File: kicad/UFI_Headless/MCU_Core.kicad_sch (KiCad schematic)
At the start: 43 parts, among them J4 SWD, J5 DBG_UART, SW1 RESET, SW2 BOOT, U5 STM32H723ZGT6, Y1 25MHz CL=8pF

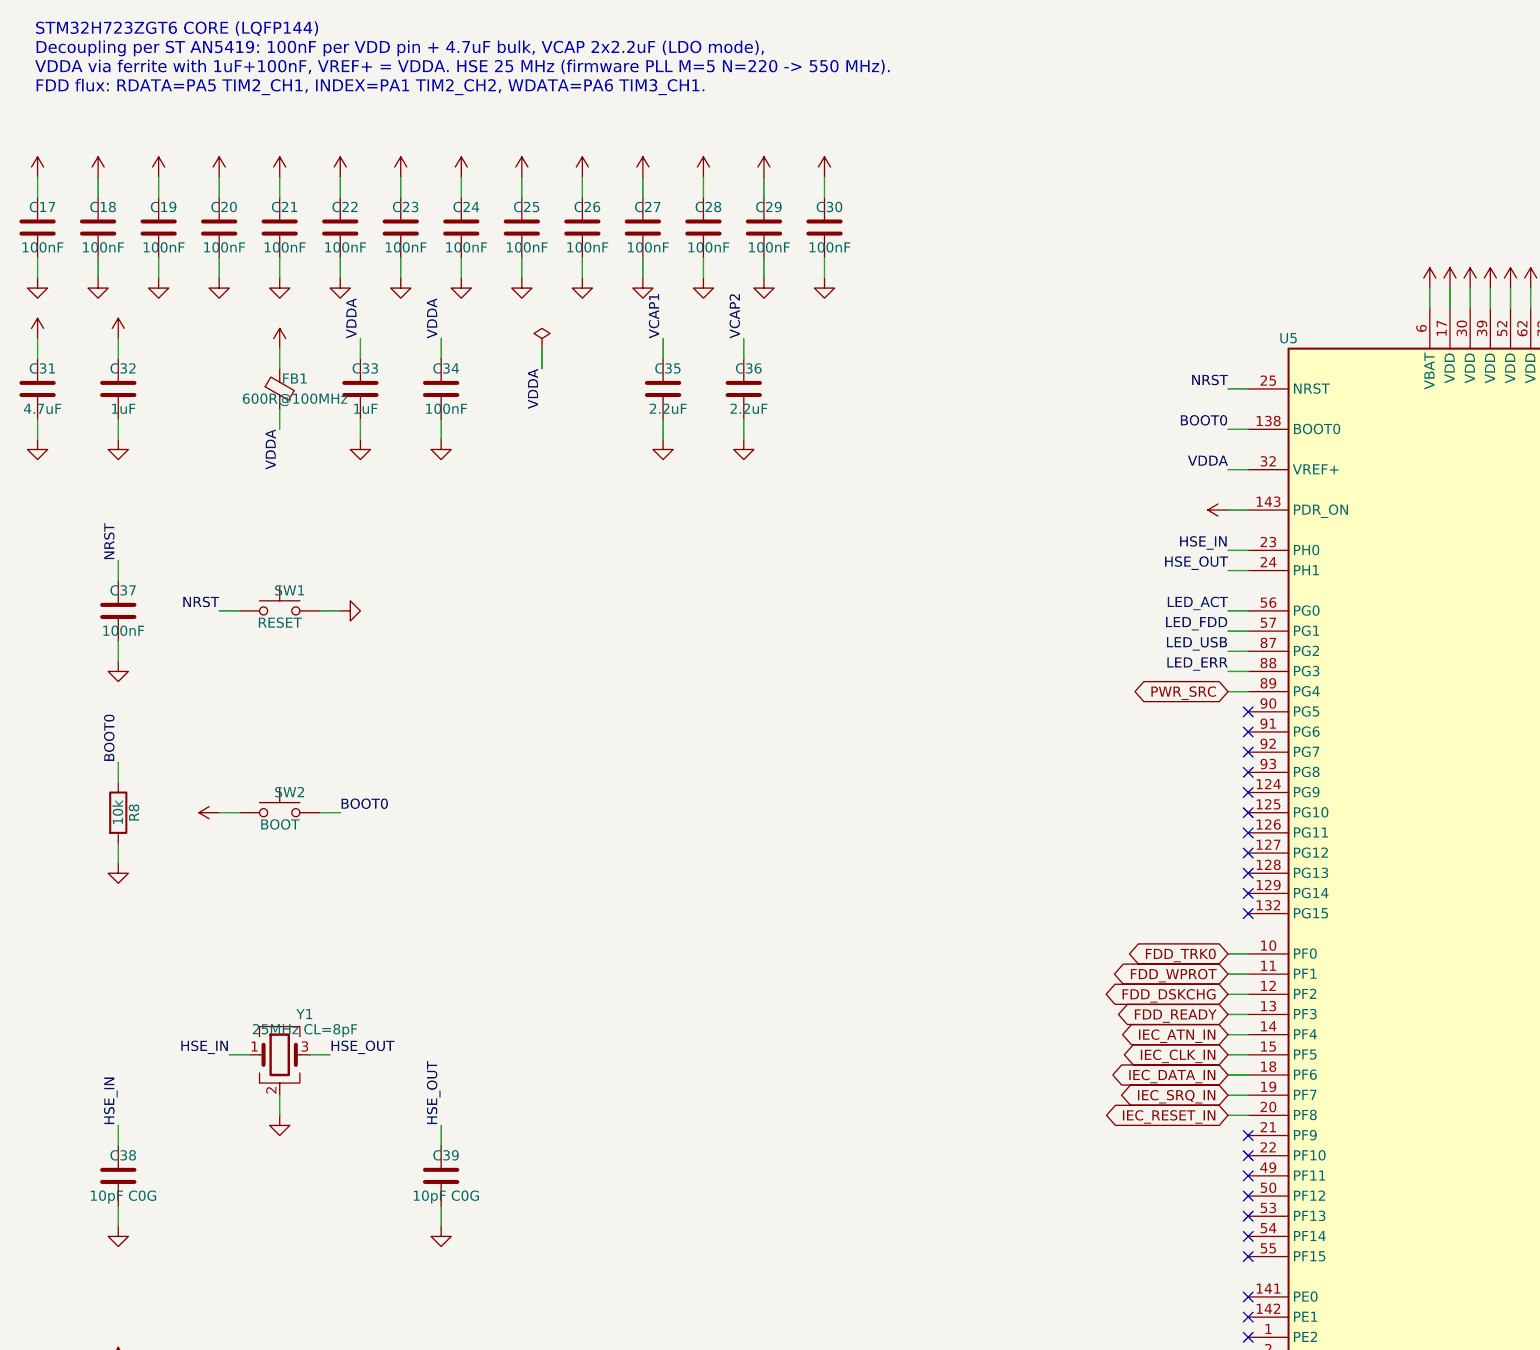
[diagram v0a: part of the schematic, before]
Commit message: UFI Headless: 4-layer layout v0.1, LCSC sourcing, fab outputs
- build_pcb.py: footprints from the schematic netlist (KIID-linked), placement,
  pre-routed USB-C fan-out and MCU VSS stubs, In1 GND plane
- make_pcb.sh: Freerouting 2.4.1 routing, violation cleanup, supply widening,
  GND/3V3 pours, stitching vias; DRC 0 errors, schematic parity clean
- LCSC part numbers via JLCPCB API; crystal X322525MOB4SI (CL 12pF, 2x 18pF)
- fertigung/: Gerber, Excellon, BOM/CPL (KiCad + JLC format)

Co-Authored-By: Claude Opus 5.5 <noreply@anthropic.com>
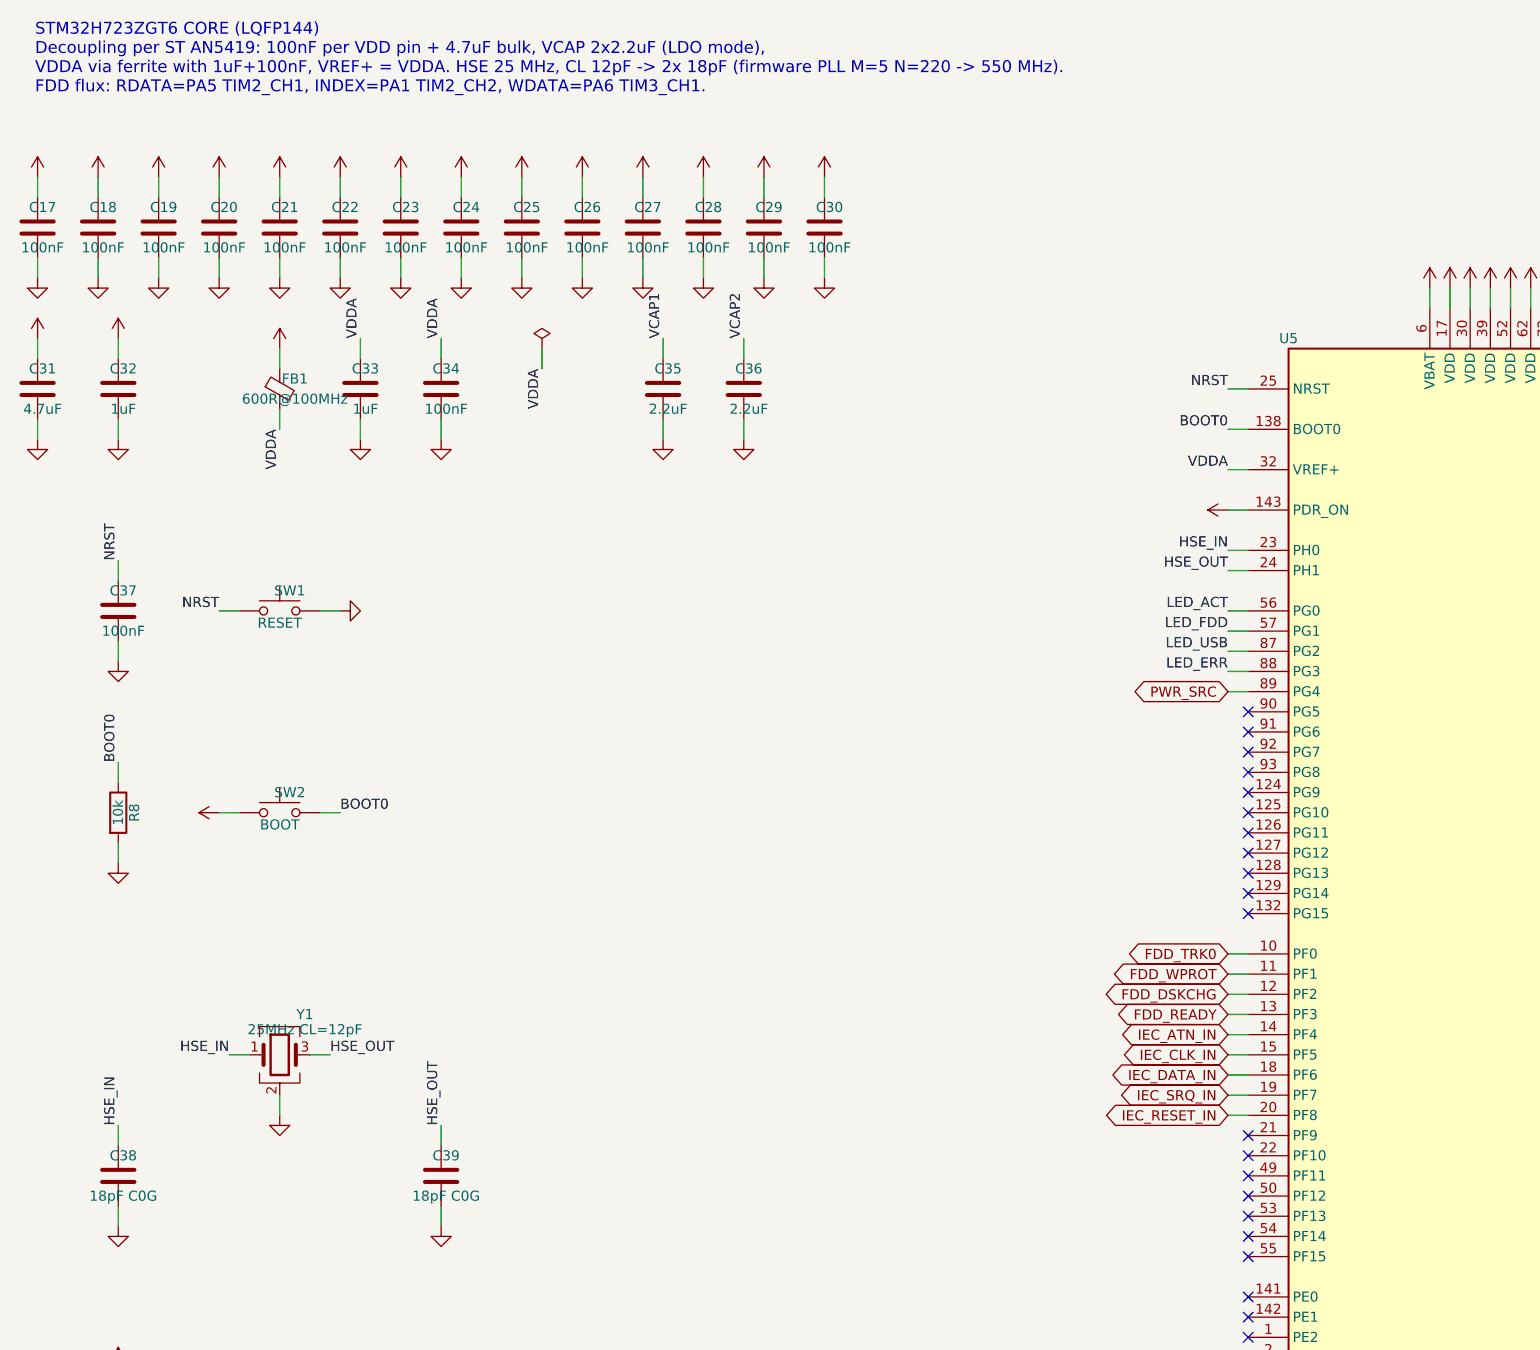
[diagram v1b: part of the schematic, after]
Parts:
- C17, C18, C19, C20, C21, C22, C23, C24, C25, C26, C27, C28, C29, C30, C34, C37: LCSC (none) -> C14663
- C31: LCSC (none) -> C1779
- C32: LCSC (none) -> C28323
- C33: LCSC (none) -> C15849
- C35, C36: LCSC (none) -> C87994
- C38, C39: value 10pF C0G -> 18pF C0G; LCSC (none) -> C1647
- D4, D5, D6, D8: LCSC (none) -> C12624
- D7: LCSC (none) -> C2286
- FB1: LCSC (none) -> C1002
- J4: LCSC (none) -> C22438120
- J5: LCSC (none) -> C49257
- R10: LCSC (none) -> C4216
- R11, R12, R13, R14: LCSC (none) -> C21190
- R15: LCSC (none) -> C4190
- R8: LCSC (none) -> C25804
- R9: LCSC (none) -> C31850
- SW1, SW2: LCSC (none) -> C2886898
- U5: LCSC (none) -> C730146
- Y1: value 25MHz CL=8pF -> 25MHz CL=12pF; LCSC (none) -> C9006; MPN 25MHz 3225 CL=8pF +-20ppm -> YXC X322525MOB4SI (25MHz, CL 12pF, +-10ppm)
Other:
- note added: "STM32H723ZGT6 CORE (LQFP144) Decoupling per ST AN5419: 100nF per VDD pin + 4.7uF bulk, VCAP 2x2.2uF (LDO mode), VDDA via ferrite with 1uF+100nF, VREF+ = VDDA. HSE 25 MHz, CL 12pF -> 2x 18pF (firmware PLL M=5 N=220 -> 550 MHz). FDD flux: RDATA=PA5 TIM2_CH1, INDEX=PA1 TIM2_CH2, WDATA=PA6 TIM3_CH1."
- note removed: "STM32H723ZGT6 CORE (LQFP144) Decoupling per ST AN5419: 100nF per VDD pin + 4.7uF bulk, VCAP 2x2.2uF (LDO mode), VDDA via ferrite with 1uF+100nF, VREF+ = VDDA. HSE 25 MHz (firmware PLL M=5 N=220 -> 550 MHz). FDD flux: RDATA=PA5 TIM2_CH1, INDEX=PA1 TIM2_CH2, WDATA=PA6 TIM3_CH1."

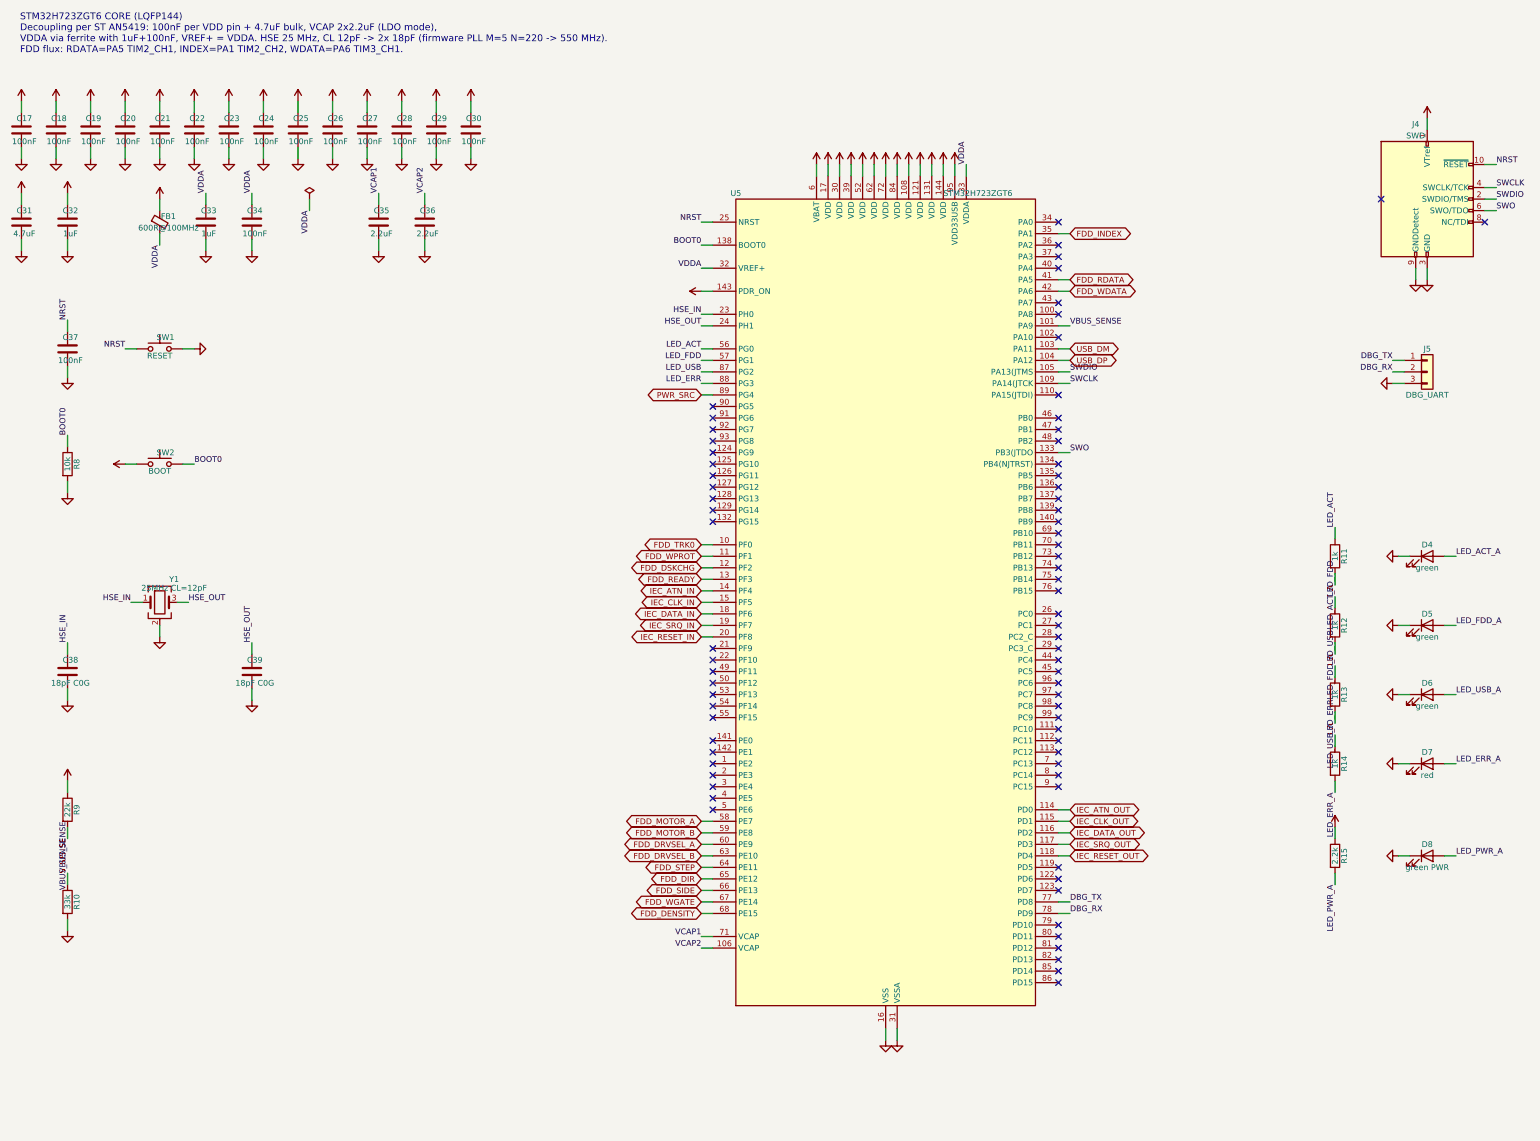
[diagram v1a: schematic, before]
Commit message: UFI Headless v0.2: 8 MB PSRAM, ESD, drive polyfuses, test points
Schematic (new parts get fixed references above the v0.1 maxima, so all
existing references and PCB links stay unchanged):
- U11 APS6404L 8 MB QSPI PSRAM on OCTOSPIM P1 (PB2/PB10/PD11/PD12/PB13/
  PD13), C46, CE# pull-up R16
- D9-D11 ESDA6V1-5SC6 on the 13 Amiga J7 bus lines + MOTOR_A, D12 on IEC
- F2/F3 polyfuses: drive supplies FDD_5V/FDD_12V for J3 and J7 pins 12/23
- TP1-TP6 (3V3, 5V, 12V, GND, RDATA, INDEX), excluded from BOM/CPL
Layout (incremental ECO on the reviewed board):
- scripts/add_parts.py: re-net pads, collision-aware placement, rip up only
  what is in the way; make_pcb.sh 'eco' step
- fixes found on the way: supply pours ran after finish_pcb and left GND
  islands (LDO U4 ground!) without vias -> order swapped, GND pour check
  per net; island/dogbone vias never inside pads; manual_routes no longer
  re-applies the D+ fallback; pipeline filters robust against interleaved
  SWIG noise under pipefail
- DRC rule for the intentional J6/J7 silk overhang instead of warnings;
  netclasses cover the new drive supply nets
DRC: 0 errors, 0 warnings, 0 unconnected, parity clean, no via-in-pad.

Co-Authored-By: Claude Opus 5.5 <noreply@anthropic.com>
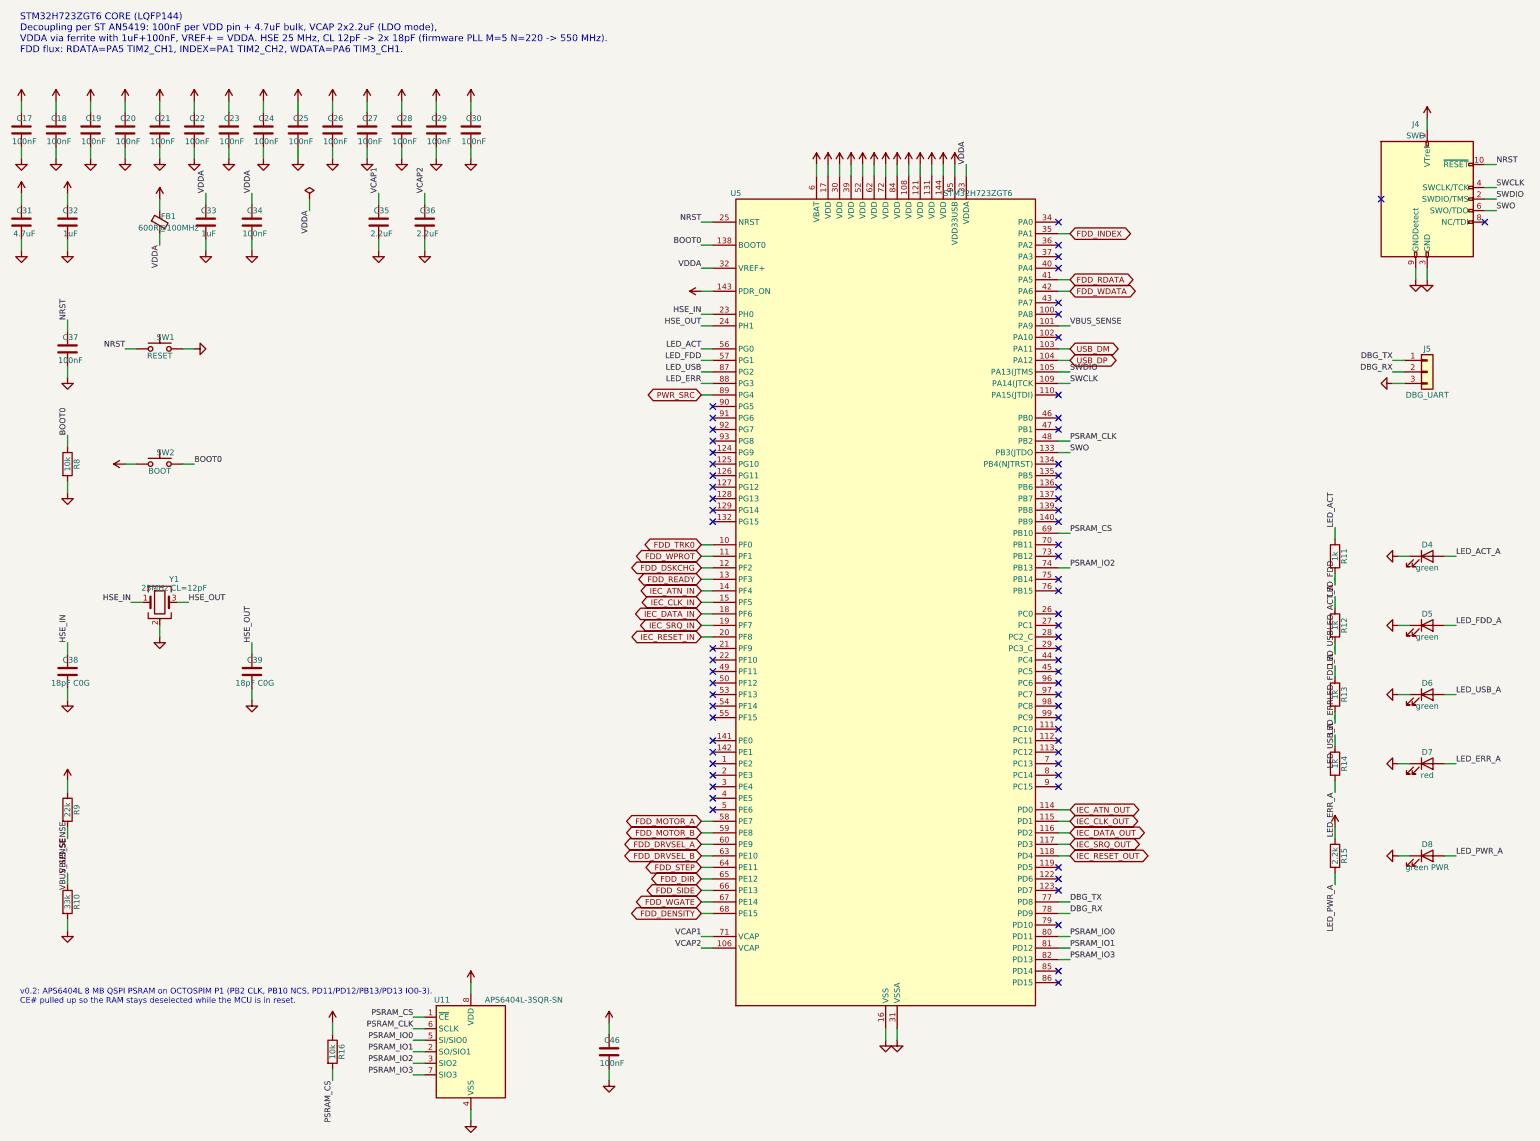
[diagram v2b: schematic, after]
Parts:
- added C46: 100nF, Capacitor_SMD:C_0603_1608Metric, symbol Device:C
- added R16: 10k, Resistor_SMD:R_0603_1608Metric, symbol Device:R
- added U11: APS6404L-3SQR-SN, Package_SO:SOIC-8_3.9x4.9mm_P1.27mm, symbol Memory_RAM:APS6404L-3SQRx-SN
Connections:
- net +3V3: now also C46.1, R16.1, U11.8 (VDD)
- net GND: now also C46.2, U11.4 (VSS)
- net PSRAM_CLK: now reaches U5.48 (PB2)
- net PSRAM_CLK: now also U11.6 (SCLK)
- net PSRAM_CS: now reaches U5.69 (PB10)
- net PSRAM_CS: now also R16.2, U11.1 (~{CE})
- net PSRAM_IO2: now reaches U5.74 (PB13)
- net PSRAM_IO2: now also U11.3 (SIO2)
- net PSRAM_IO0: now reaches U5.80 (PD11)
- net PSRAM_IO0: now also U11.5 (SI/SIO0)
- net PSRAM_IO1: now reaches U5.81 (PD12)
- net PSRAM_IO1: now also U11.2 (SO/SIO1)
- net PSRAM_IO3: now reaches U5.82 (PD13)
- net PSRAM_IO3: now also U11.7 (SIO3)
- no-connect marks 75 -> 69
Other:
- note added: "v0.2: APS6404L 8 MB QSPI PSRAM on OCTOSPIM P1 (PB2 CLK, PB10 NCS, PD11/PD12/PB13/PD13 IO0-3). CE# pulled up so the RAM stays deselected while the MCU is in reset."

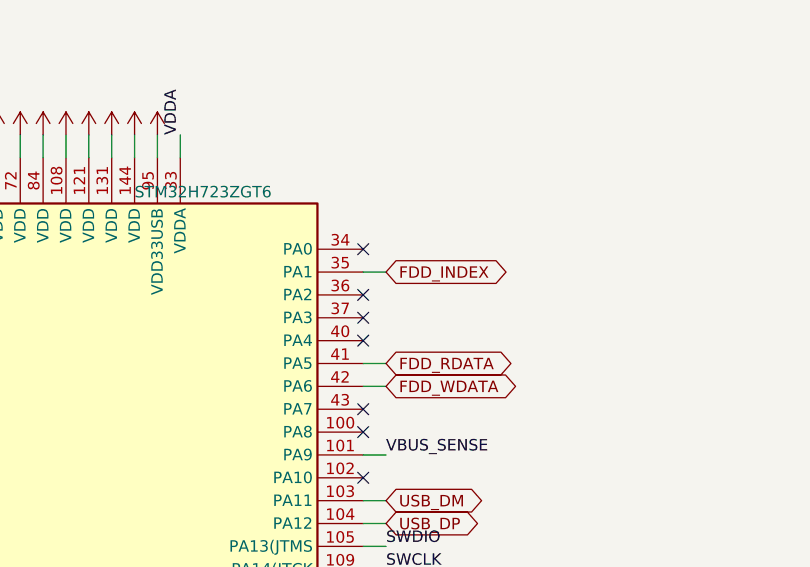
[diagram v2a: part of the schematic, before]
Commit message: UFI Headless v0.3: USB-C source current detection
- schematic: CC1/CC2 (Rd 5.1k) also to PA0/PA3 (ADC1 INP16/INP15); ECO
  routed on the reviewed board, DRC 0 errors / 0 warnings, parity clean
- firmware: USB_POWER (0x19) measures CC voltages, reports the allowed
  source current (0.5 / 1.5 / 3 A per Type-C vRd ranges)
- host tool: ufi usb-power
- manual_routes: D+ fallback skipped when any D+ via is near its start
  (Freerouting's own via sits 0.25 mm away; it was re-added every run)
- README: CC pins, Atari SIO option on existing UART pins (PD1/PF6/PD0)

Co-Authored-By: Claude Opus 5.5 <noreply@anthropic.com>
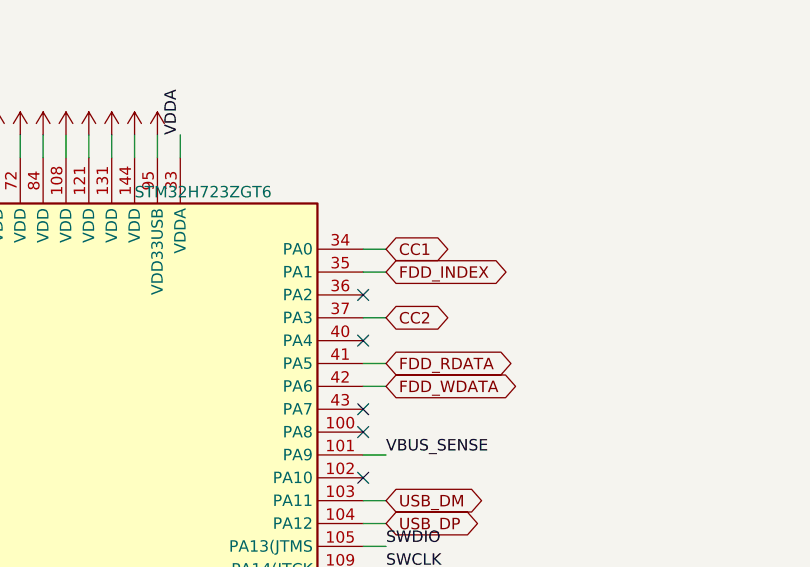
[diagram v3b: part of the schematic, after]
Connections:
- net CC1: now reaches U5.34 (PA0)
- net CC2: now reaches U5.37 (PA3)
- no-connect marks 69 -> 67
